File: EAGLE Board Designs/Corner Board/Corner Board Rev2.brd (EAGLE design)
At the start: 100 x 50 mm, 31 parts, among them J1 CONNECTOR-8_AMPHENOL_M12A_08P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, J2 CONNECTOR-2_MICROFIT_SMD_RIGH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, J3 CONNECTOR-8_AMPHENOL_M12A_08P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, J4 CONNECTOR-4_μF_S_RA_, J5 CONNECTOR-4_μF_S_RA_, U1 VOLTAGE_REGULATOR_SOT-89_15V, U2 OPAMP_1_CHANNEL_OPA991, U3 INA823DT, U4 OPAMP_1_CHANNEL_OPA991, U5 OPAMP_1_CHANNEL_OPA991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

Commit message: moved info silk to bottom
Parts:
- added U$15: (no value), HyTechManufacturing:LOGO_GT_LARGE
- added U$6: (no value), HyTechManufacturing:LOGO_HYTECH_LARGE
- moved U$14 62.8 mm to (12.8, 18.9)
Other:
- board text added: "Corner Board rev2 Designed by: Liwei Sun Shayan Noorani Mikhail Allen"
- board text removed: "Corner Board rev2 Designed by: Liwei Sun Shayan Noorani"
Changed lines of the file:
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@@
 <layer number="17" name="Pads" color="2" fill="1" visible="yes" active="yes"/>
 <layer number="18" name="Vias" color="2" fill="1" visible="yes" active="yes"/>
-<layer number="19" name="Unrouted" color="6" fill="1" visible="no" active="yes"/>
+<layer number="19" name="Unrouted" color="6" fill="1" visible="yes" active="yes"/>
 <layer number="20" name="Dimension" color="24" fill="1" visible="yes" active="yes"/>
 <layer number="21" name="tPlace" color="7" fill="1" visible="yes" active="yes"/>
@@
 <layer number="25" name="tNames" color="7" fill="1" visible="yes" active="yes"/>
 <layer number="26" name="bNames" color="7" fill="1" visible="yes" active="yes"/>
-<layer number="27" name="tValues" color="7" fill="1" visible="yes" active="yes"/>
-<layer number="28" name="bValues" color="7" fill="1" visible="yes" active="yes"/>
-<layer number="29" name="tStop" color="7" fill="3" visible="yes" active="yes"/>
+<layer number="27" name="tValues" color="7" fill="1" visible="no" active="yes"/>
+<layer number="28" name="bValues" color="7" fill="1" visible="no" active="yes"/>
+<layer number="29" name="tStop" color="7" fill="3" visible="no" active="yes"/>
 <layer number="30" name="bStop" color="7" fill="6" visible="no" active="yes"/>
 <layer number="31" name="tCream" color="7" fill="4" visible="no" active="yes"/>
@@
 <layer number="41" name="tRestrict" color="4" fill="10" visible="yes" active="yes"/>
 <layer number="42" name="bRestrict" color="1" fill="10" visible="yes" active="yes"/>
-<layer number="43" name="vRestrict" color="2" fill="10" visible="yes" active="yes"/>
+<layer number="43" name="vRestrict" color="2" fill="10" visible="no" active="yes"/>
 <layer number="44" name="Drills" color="7" fill="1" visible="no" active="yes"/>
-<layer number="45" name="Holes" color="7" fill="1" visible="yes" active="yes"/>
+<layer number="45" name="Holes" color="7" fill="1" visible="no" active="yes"/>
 <layer number="46" name="Milling" color="3" fill="1" visible="no" active="yes"/>
 <layer number="47" name="Measures" color="7" fill="1" visible="no" active="yes"/>
-<layer number="48" name="Document" color="7" fill="1" visible="yes" active="yes"/>
-<layer number="49" name="Reference" color="7" fill="1" visible="yes" active="yes"/>
+<layer number="48" name="Document" color="7" fill="1" visible="no" active="yes"/>
+<layer number="49" name="Reference" color="7" fill="1" visible="no" active="yes"/>
 <layer number="50" name="dxf" color="7" fill="1" visible="no" active="no"/>
 <layer number="51" name="tDocu" color="7" fill="1" visible="yes" active="yes"/>
@@
 <layer number="155" name="FabDoc3" color="7" fill="1" visible="no" active="yes"/>
 <layer number="156" name="HVSpacing" color="12" fill="1" visible="no" active="yes"/>
-<layer number="157" name="HIGH_VOLTAGE_WIRES" color="2" fill="1" visible="yes" active="yes"/>
+<layer number="157" name="HIGH_VOLTAGE_WIRES" color="2" fill="1" visible="no" active="yes"/>
 <layer number="166" name="AntennaArea" color="7" fill="1" visible="no" active="no"/>
 <layer number="168" name="4mmHeightArea" color="7" fill="1" visible="no" active="no"/>
@@
 <wire x1="100" y1="50" x2="0" y2="50" width="0" layer="20"/>
 <wire x1="0" y1="50" x2="0" y2="0" width="0" layer="20"/>
-<text x="14.732" y="15.748" size="1.27" layer="21" font="vector">Corner Board rev2
+<text x="90.424" y="7.366" size="1.27" layer="22" font="vector" rot="MR0">Corner Board rev2
 Designed by:
 Liwei Sun
-Shayan Noorani</text>
+Shayan Noorani
+Mikhail Allen</text>
 <polygon width="0.254" layer="29">
 <vertex x="5" y="8"/>
@@
 </element>
 <element name="U$13" library="HyTechManufacturing" package="LOGO_HYTECH_MEDIUM" value="" x="7.239" y="6.985" smashed="yes"/>
-<element name="U$14" library="HyTechManufacturing" package="LOGO_GT_MEDIUM" value="" x="75.057" y="10.287" smashed="yes"/>
+<element name="U$14" library="HyTechManufacturing" package="LOGO_GT_MEDIUM" value="" x="12.827" y="18.923" smashed="yes"/>
+<element name="U$6" library="HyTechManufacturing" package="LOGO_HYTECH_LARGE" value="" x="58.928" y="27.432" smashed="yes" rot="MR0"/>
+<element name="U$15" library="HyTechManufacturing" package="LOGO_GT_LARGE" value="" x="32.512" y="16.51" smashed="yes" rot="MR0"/>
 </elements>
 <signals>

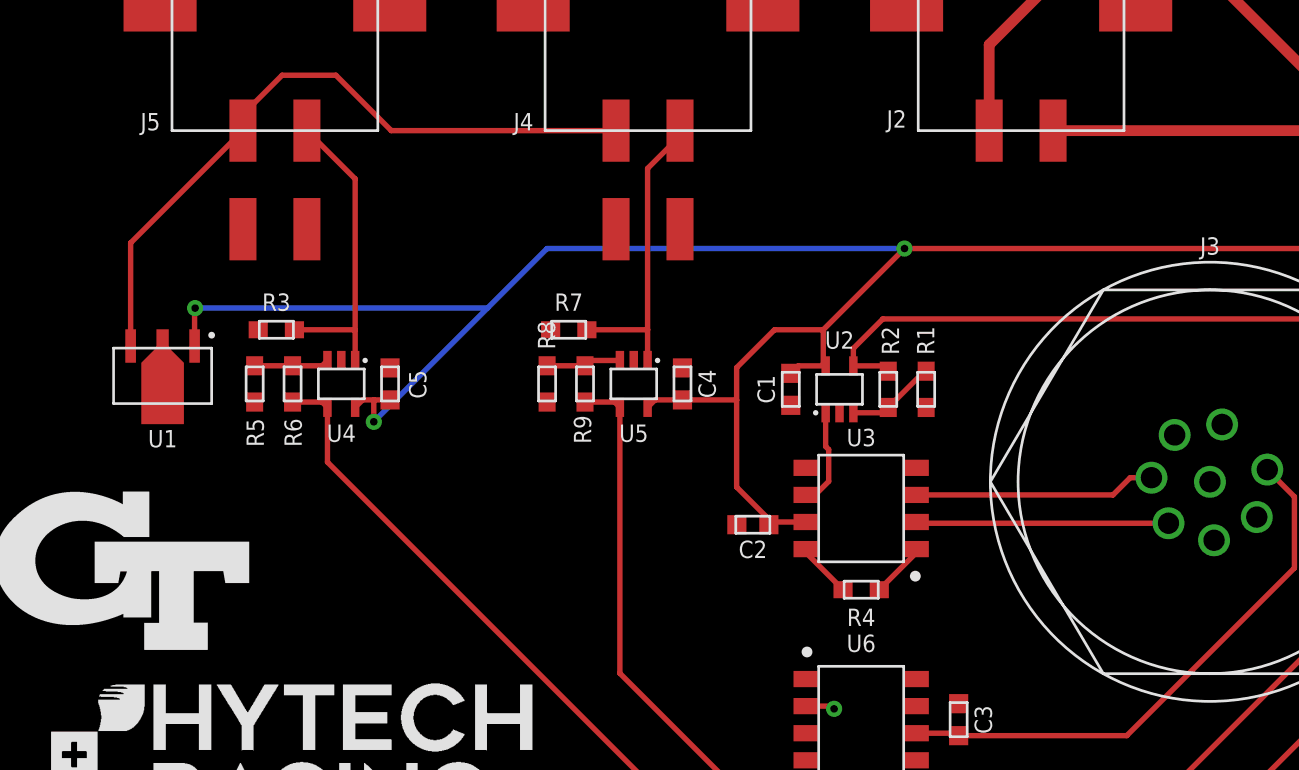
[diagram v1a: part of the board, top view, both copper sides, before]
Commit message: switched to 15v and added jumps for signals
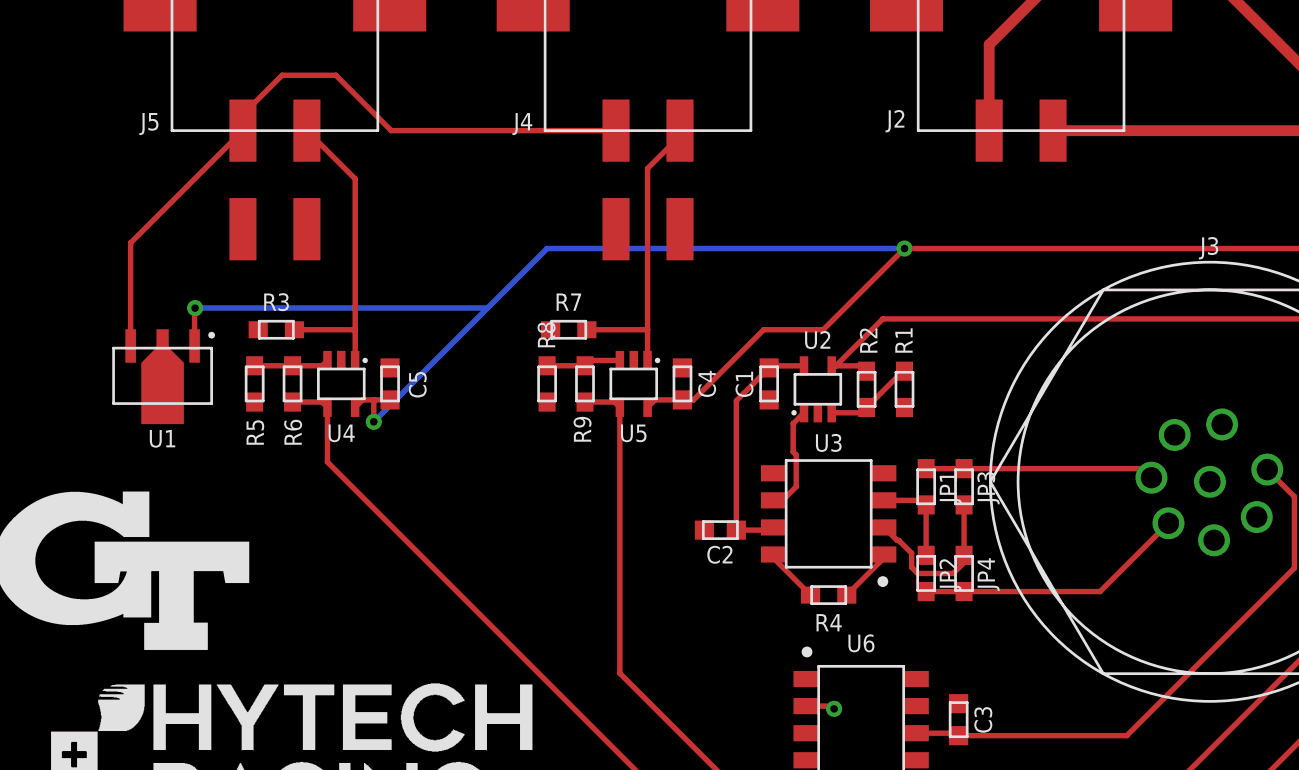
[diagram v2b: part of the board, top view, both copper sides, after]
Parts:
- added JP1, JP2, JP3, JP4: JUMPER_0603_, HyTechDevices:0603-RES
- moved C2 1.55 mm to (40.9, 20.8)
- moved U3 1.55 mm to (46.0, 21.6)
- moved R4 1.55 mm to (46.0, 17.8)
- moved C1 1.05 mm to (43.2, 27.7)
- moved R1 1.02 mm to (49.5, 27.4)
- moved R2 1.02 mm to (47.8, 27.4)
- moved U2 1.02 mm to (45.5, 27.4)
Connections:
- new net N$6: JP1.2, JP2.1, U3.3
- new net N$7: JP3.2, JP4.1, U3.2
- net +24V: no longer C1.1, C2.1, U2.5, U3.7
- net 15V: now also C1.1, C2.1, U2.5, U3.7
- net SIGNAL+: now also JP1.1, JP3.1; no longer U3.3
- net SIGNAL-: now also JP2.2, JP4.2; no longer U3.2
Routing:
- net +24V: track 122.5 -> 109.9 mm
- net 15V: track 32.4 -> 44.1 mm
- net N$7: track 0.00 -> 7.95 mm
- net N$6: track 0.00 -> 4.42 mm
- net SIGNAL-: track 11.8 -> 12.7 mm
- net SIGNAL+: track 11.3 -> 10.7 mm
- net LOAD_CELL_AMPLIFIED: track 45.0 -> 45.5 mm

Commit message: added pullup pulldown and dc offset
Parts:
- added C6: CAPACITOR_0603_25V_1UF, HyTechDevices:0603-CAP
- added R10, R11, R12: RESISTOR_0603_1.5M, HyTechDevices:0603-RES
- added R14: RESISTOR_0603_30K, HyTechDevices:0603-RES
- moved C2 2.29 mm to (38.6, 20.8)
- moved R4 2.29 mm to (43.7, 17.8)
- moved U3 2.29 mm to (43.7, 21.6)
- moved U1 0.25 mm to (14.7, 29.7)
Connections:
- new net N$9: JP1.2, JP2.1, R11.1, U3.3
- net +24V: now also R11.2
- net 15V: now also R12.2
- net GND: now also R10.1, R14.1
- net LOAD_CELL_AMPLIFIED: now also C6.1, R12.1, R14.2; no longer R2.2, U2.4
- net N$6: now also C6.2, R2.2, U2.4; no longer JP1.2, JP2.1, U3.3
- net N$7: now also R10.2
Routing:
- net 15V: track 44.1 -> 89.1 mm, vias 0 -> 2
- net +24V: track 109.9 -> 135.8 mm, vias 4 -> 5
- net N$9: track 0.00 -> 6.74 mm
- net LOAD_CELL_AMPLIFIED: track 45.5 -> 38.8 mm
- net N$7: track 7.95 -> 9.84 mm
- net SUS_POT_1_24V: track 72.5 -> 73.4 mm
- net N$3: track 5.08 -> 5.91 mm
- net PREINTERLOCK: track 78.3 -> 77.6 mm

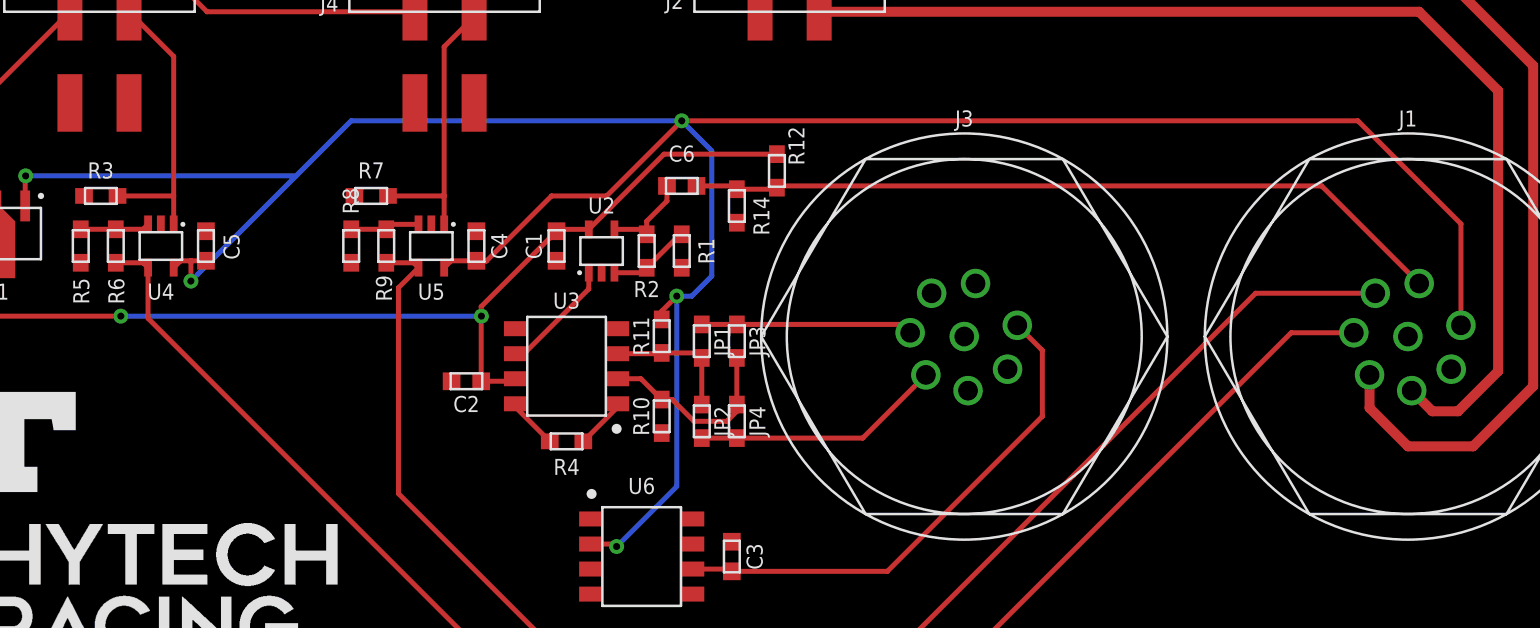
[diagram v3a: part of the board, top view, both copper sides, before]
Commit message: new dc offset and new gain
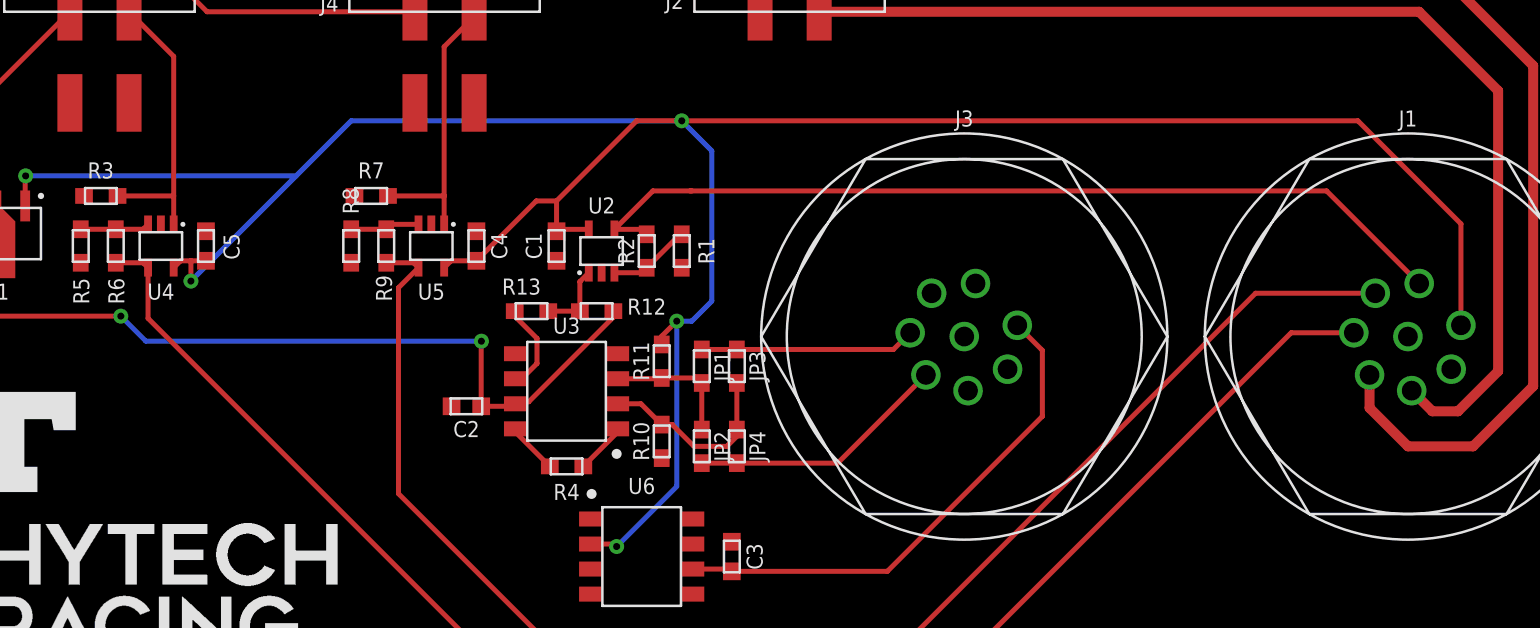
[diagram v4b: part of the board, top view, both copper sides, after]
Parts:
- removed C6: CAPACITOR_0603_25V_1UF, HyTechDevices:0603-CAP
- removed R14: RESISTOR_0603_30K, HyTechDevices:0603-RES
- added R13: RESISTOR_0603_1K, HyTechDevices:0603-RES
- R12: value RESISTOR_0603_1.5M -> RESISTOR_0603_1M
- R2: value RESISTOR_0603_22.1K -> RESISTOR_0603_20K
- moved R12 11.6 mm to (45.2, 24.4), turned to 0 degrees
- moved C2 1.27 mm to (38.6, 19.6)
- moved JP1 1.27 mm to (50.5, 21.6)
- moved JP2 1.27 mm to (50.5, 17.5)
- moved JP3 1.27 mm to (52.3, 21.6)
- moved JP4 1.27 mm to (52.3, 17.5)
- moved R10 1.27 mm to (48.5, 17.8)
- moved R11 1.27 mm to (48.5, 21.8)
- moved R4 1.27 mm to (43.7, 16.5)
- moved U3 1.27 mm to (43.7, 20.3)
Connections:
- net +24V: now also C1.1, U2.5
- net 15V: no longer C1.1, U2.5
- net GND: no longer R14.1
- net LOAD_CELL_AMPLIFIED: now also R2.2, U2.4; no longer C6.1, R12.1, R14.2
- net N$3: now also R13.1; no longer U2.1
- net N$6: now also R12.1, R13.2, U2.1; no longer C6.2, R2.2, U2.4
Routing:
- net 15V: track 89.1 -> 78.1 mm
- net LOAD_CELL_AMPLIFIED: track 38.8 -> 45.4 mm
- net +24V: track 135.8 -> 139.0 mm
- net N$3: track 5.91 -> 4.83 mm
- net N$6: track 4.62 -> 3.74 mm
- net SIGNAL-: track 12.7 -> 13.2 mm

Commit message: post review
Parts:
- added C6: CAPACITOR_0805_25V_22UF, HyTechDevices:0805-CAP
- added CV1: 2.2uF, HyTechDevices:0603-CAP
- moved C5 1.52 mm to (26.9, 27.7)
- moved R3 1.52 mm to (21.6, 30.2)
- moved R5 1.52 mm to (20.6, 27.7)
- moved R6 1.52 mm to (22.4, 27.7)
- moved U4 1.52 mm to (24.6, 27.7)
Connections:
- net +24V: now also CV1.1
- net 10V: now also J3.7; no longer J3.1
- net 15V: now also C6.1
- net GND: now also C6.2, CV1.2
- net SIGNAL+: now also J3.3; no longer J3.4
- net SIGNAL-: now also J3.4; no longer J3.5
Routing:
- net +24V: track 139.0 -> 144.5 mm
- net 10V: track 26.2 -> 22.7 mm
- net 15V: track 78.1 -> 81.5 mm
- net SIGNAL+: track 10.9 -> 12.8 mm
- net SUS_POT_2_24V: track 79.8 -> 79.2 mm
- net SUS_POT_2: track 14.6 -> 15.2 mm

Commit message: post post review
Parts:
- removed CV1: 2.2uF, HyTechDevices:0603-CAP
- added C7: CAPACITOR_0603_50V_1UF, HyTechDevices:0603-CAP
- added C8: CAPACITOR_0603_50V_0.1UF, HyTechDevices:0603-CAP
- moved C5 1.52 mm to (28.4, 27.7)
- moved R3 1.52 mm to (23.1, 30.2)
- moved R6 1.52 mm to (23.9, 27.7)
- moved R5 1.52 mm to (22.1, 27.7)
- moved U4 1.52 mm to (26.2, 27.7)
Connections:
- net +24V: now also C7.1, C8.1; no longer CV1.1
- net GND: now also C7.2, C8.2; no longer CV1.2
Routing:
- net +24V: track 144.5 -> 145.7 mm
- net SUS_POT_2_24V: track 79.2 -> 78.5 mm
